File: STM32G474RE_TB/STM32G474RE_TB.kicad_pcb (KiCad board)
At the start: 2 copper layers, 37 parts, among them SW1 TS-1088-AR02016, U1 STM32G474RETx, U10 L7805, U2 XC6206P332MR-G, U3 REF3125, U4 MCP4921-ESN, U5 OPA1678, U6 OPA1678, U7 MCP4921-ESN, U8 MCP4921-ESN, U9 MCP4921-ESN, Y1 ABM8G-24.000MHZ-18-D2Y-T

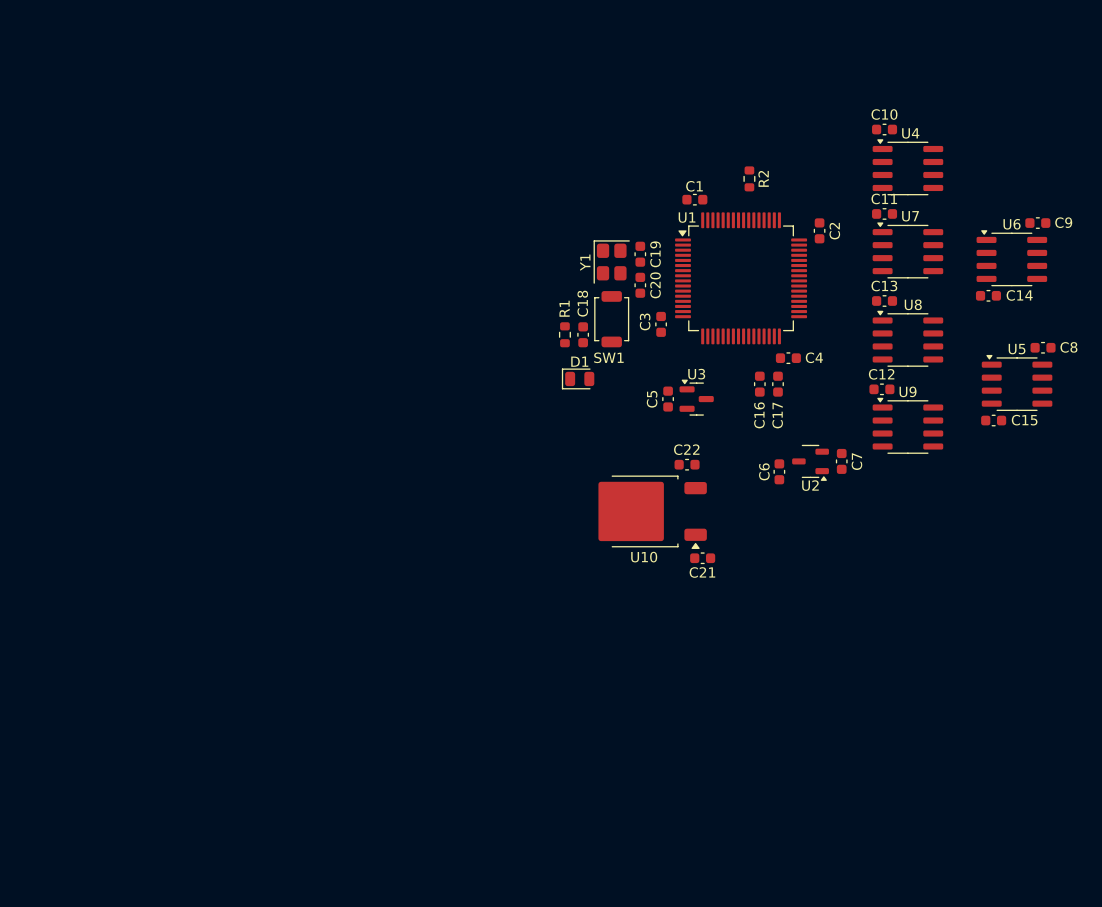
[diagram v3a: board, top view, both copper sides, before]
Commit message: Adjusted layouts and added DAC buffer from stm32.
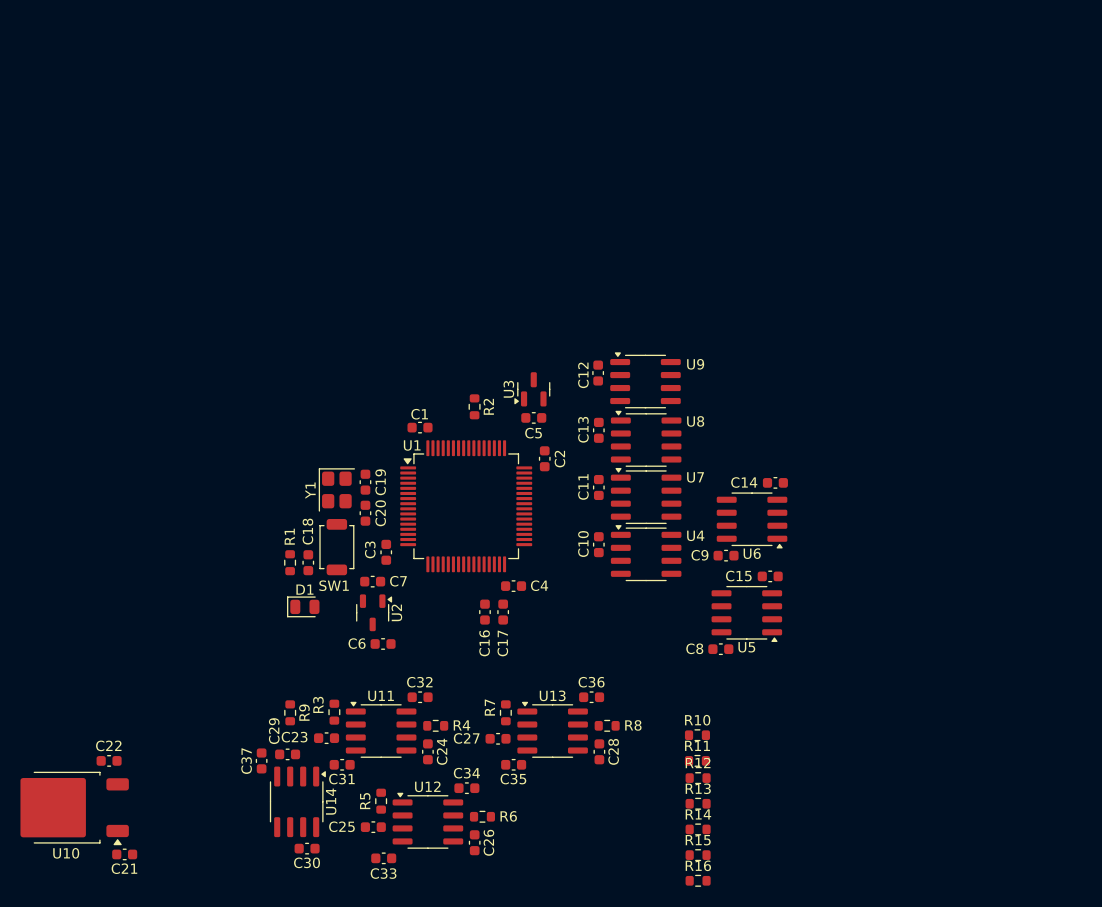
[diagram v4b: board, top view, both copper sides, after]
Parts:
- added C23: 330nF, Capacitor_SMD:C_0603_1608Metric, F.Cu at (57.5, 90.0)
- added C24: 330nF, Capacitor_SMD:C_0603_1608Metric, F.Cu at (67.4, 91.3)
- added C25: 330nF, Capacitor_SMD:C_0603_1608Metric, F.Cu at (62.0, 98.7)
- added C26: 330nF, Capacitor_SMD:C_0603_1608Metric, F.Cu at (71.9, 100.2)
- added C27: 330nF, Capacitor_SMD:C_0603_1608Metric, F.Cu at (74.2, 90.0)
- added C28: 33nf, Capacitor_SMD:C_0603_1608Metric, F.Cu at (84.1, 91.3)
- added C29: 33nf, Capacitor_SMD:C_0603_1608Metric, F.Cu at (53.7, 91.6)
- added C30: 0.1uf, Capacitor_SMD:C_0603_1608Metric, F.Cu at (55.6, 100.8)
- added C31: 0.1uf, Capacitor_SMD:C_0603_1608Metric, F.Cu at (59.0, 92.6)
- added C32: 0.1uf, Capacitor_SMD:C_0603_1608Metric, F.Cu at (66.6, 86.0)
- added C33: 0.1uf, Capacitor_SMD:C_0603_1608Metric, F.Cu at (63.1, 101.7)
- added C34: 0.1uf, Capacitor_SMD:C_0603_1608Metric, F.Cu at (71.2, 94.9)
- added C35: 0.1uf, Capacitor_SMD:C_0603_1608Metric, F.Cu at (75.8, 92.6)
- added C36: 0.1uf, Capacitor_SMD:C_0603_1608Metric, F.Cu at (83.4, 86.0)
- added C37: 0.1uf, Capacitor_SMD:C_0603_1608Metric, F.Cu at (51.1, 92.2)
- added R10: 1k, Resistor_SMD:R_0603_1608Metric, F.Cu at (93.7, 89.7)
- added R11: 1k, Resistor_SMD:R_0603_1608Metric, F.Cu at (93.7, 92.2)
- added R12: 1k, Resistor_SMD:R_0603_1608Metric, F.Cu at (93.8, 93.9)
- added R13: 1k, Resistor_SMD:R_0603_1608Metric, F.Cu at (93.8, 96.4)
- added R14: 1k, Resistor_SMD:R_0603_1608Metric, F.Cu at (93.8, 98.9)
- added R15: 1k, Resistor_SMD:R_0603_1608Metric, F.Cu at (93.8, 101.4)
- added R16: 1k, Resistor_SMD:R_0603_1608Metric, F.Cu at (93.8, 103.9)
- added R3: 220, Resistor_SMD:R_0603_1608Metric, F.Cu at (58.2, 87.4)
- added R4: 220, Resistor_SMD:R_0603_1608Metric, F.Cu at (68.1, 88.8)
- added R5: 220, Resistor_SMD:R_0603_1608Metric, F.Cu at (62.8, 96.1)
- added R6: 220, Resistor_SMD:R_0603_1608Metric, F.Cu at (72.7, 97.7)
- added R7: 220, Resistor_SMD:R_0603_1608Metric, F.Cu at (75.0, 87.5)
- added R8: 220, Resistor_SMD:R_0603_1608Metric, F.Cu at (84.9, 88.8)
- added R9: 220, Resistor_SMD:R_0603_1608Metric, F.Cu at (53.9, 87.5)
- added U11: OPA1678, Package_SO:SOIC-8_3.9x4.9mm_P1.27mm, F.Cu at (62.8, 89.3)
- added U12: OPA1678, Package_SO:SOIC-8_3.9x4.9mm_P1.27mm, F.Cu at (67.4, 98.2)
- added U13: OPA1678, Package_SO:SOIC-8_3.9x4.9mm_P1.27mm, F.Cu at (79.6, 89.3)
- added U14: OPA1678, Package_SO:SOIC-8_3.9x4.9mm_P1.27mm, F.Cu at (54.5, 96.2)
- moved U10 63.5 mm to (32.0, 96.8)
- moved C22 63.5 mm to (36.2, 92.2)
- moved C21 63.5 mm to (37.7, 101.3)
- moved C10 49.3 mm to (84.1, 71.1), turned to -90 degrees
- moved C7 47.3 mm to (62.0, 74.7), turned to 180 degrees
- moved U4 45.6 mm to (88.7, 72.0)
- moved U2 45.3 mm to (62.0, 77.7), turned to -90 degrees
- moved C9 44.6 mm to (96.5, 72.1), turned to 180 degrees
- moved C8 43.1 mm to (96.0, 81.3), turned to 180 degrees
- moved C6 42.2 mm to (63.0, 80.8), turned to 180 degrees
- moved C11 38.7 mm to (84.1, 65.5), turned to -90 degrees
- moved U6 35.9 mm to (99.1, 68.6), turned to 180 degrees
- moved U7 35.1 mm to (88.7, 66.4)
- moved C16 34.9 mm to (73.0, 77.7)
- moved C18 34.9 mm to (55.7, 72.8)
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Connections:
- U1 pad 10: unconnected-(U1-PC2-Pad10) -> /TIM1_CH3
- U1 pad 11: unconnected-(U1-PC3-Pad11) -> /TIM1_CH4
- U1 pad 12: unconnected-(U1-PA0-Pad12) -> /TIM2_SQIN
- U1 pad 13: unconnected-(U1-PA1-Pad13) -> /TIM5_CH2
- U1 pad 14: unconnected-(U1-PA2-Pad14) -> /STDAC3_C1_OUT
- U1 pad 17: unconnected-(U1-PA3-Pad17) -> /TIM5_CH4
- U1 pad 18: unconnected-(U1-PA4-Pad18) -> /STDAC1_C1_OUT
- U1 pad 19: unconnected-(U1-PA5-Pad19) -> /STDAC1_C2_OUT
- U1 pad 20: unconnected-(U1-PA6-Pad20) -> /STDAC2_OUT
- U1 pad 21: unconnected-(U1-PA7-Pad21) -> /TIM3_CH2
- U1 pad 24: unconnected-(U1-PB0-Pad24) -> /TIM3_CH3
- U1 pad 25: unconnected-(U1-PB1-Pad25) -> /STDAC3_C2_OUT
- U1 pad 26: unconnected-(U1-PB2-Pad26) -> /TIM5_CH1
- U1 pad 34: unconnected-(U1-PB12-Pad34) -> /STDAC4_C1_OUT
- U1 pad 42: unconnected-(U1-PA8-Pad42) -> /STDAC4_C2_OUT
- U1 pad 45: unconnected-(U1-PA11-Pad45) -> /TIM4_CH1
- U1 pad 46: unconnected-(U1-PA12-Pad46) -> /TIM4_CH2
- U1 pad 57: unconnected-(U1-PB4-Pad57) -> /TIM3_CH1
- U1 pad 60: unconnected-(U1-PB7-Pad60) -> /TIM3_CH4
- U1 pad 61: unconnected-(U1-PB8-Pad61) -> /TIM4_CH3
- U1 pad 62: unconnected-(U1-PB9-Pad62) -> /TIM4_CH4
- U1 pad 8: unconnected-(U1-PC0-Pad8) -> /TIM1_CH1
- U1 pad 9: unconnected-(U1-PC1-Pad9) -> /TIM1_CH2

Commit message: Added MOSFET template with led for debug or other functions
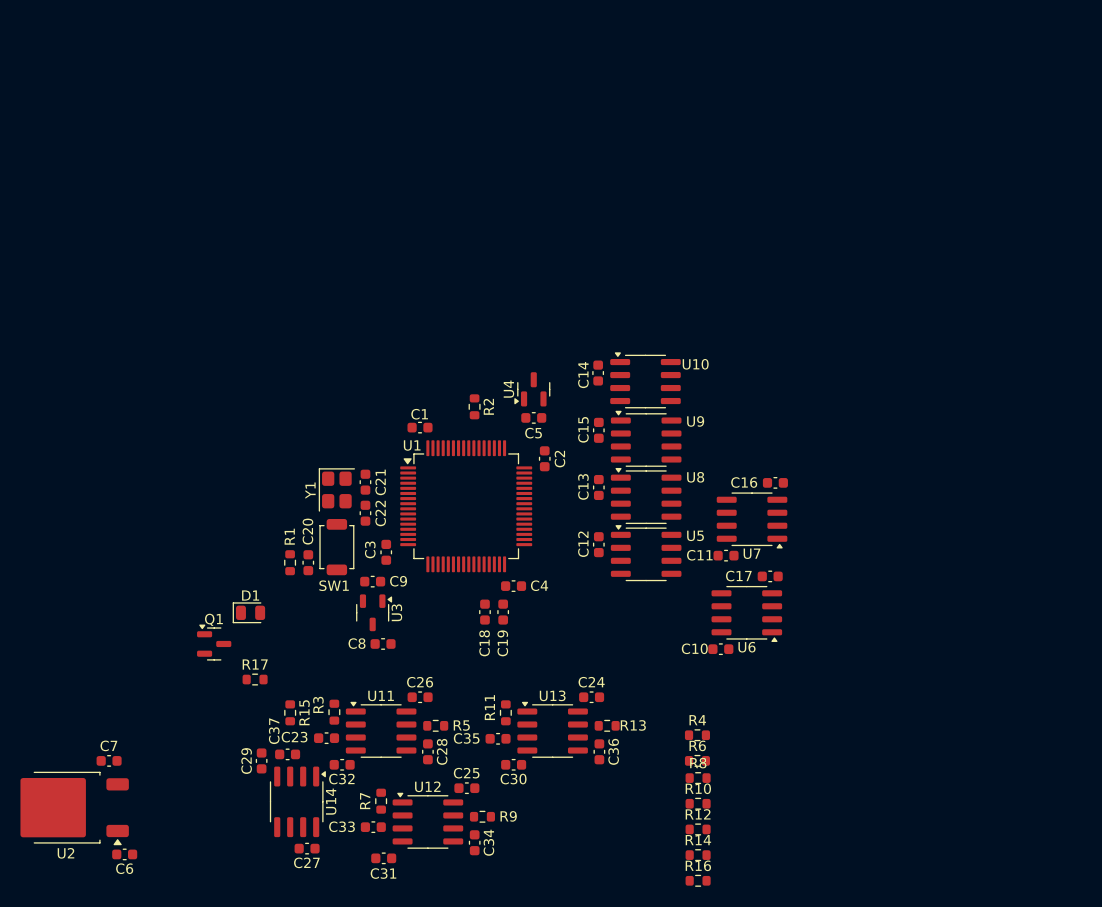
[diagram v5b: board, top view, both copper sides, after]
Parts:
- added Q1: 2N7002, Package_TO_SOT_SMD:SOT-23, F.Cu at (46.5, 80.8)
- added R17: 220, Resistor_SMD:R_0603_1608Metric, F.Cu at (50.5, 84.2)
- D1: value KT-0805G -> XL-2012UBC
- moved D1 5.34 mm to (50.0, 77.7)
- renumbered C8 to C10, C9 to C11, C10 to C12, C11 to C13, C12 to C14, C13 to C15, C14 to C16, C15 to C17, C16 to C18, C17 to C19, C18 to C20, C19 to C21, C20 to C22, C36 to C24, C34 to C25, C32 to C26, C30 to C27, C24 to C28, C37 to C29, C35 to C30, C33 to C31, C31 to C32, C25 to C33, C26 to C34, C27 to C35, C28 to C36, C29 to C37, C21 to C6, C22 to C7, C6 to C8, C7 to C9, R13 to R10, R7 to R11, R14 to R12, R8 to R13, R15 to R14, R9 to R15, R10 to R4, R4 to R5, R11 to R6, R5 to R7, R12 to R8, R6 to R9, U9 to U10, U10 to U2, U2 to U3, U3 to U4, U4 to U5, U5 to U6, U6 to U7, U7 to U8, U8 to U9
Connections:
- D1 pad 1: unconnected-(D1-K-Pad1) -> Net-(D1-K)
- D1 pad 2: unconnected-(D1-A-Pad2) -> Net-(D1-A)
